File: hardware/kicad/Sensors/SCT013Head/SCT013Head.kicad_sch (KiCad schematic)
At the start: 7 parts, among them J1 Conn_01x05_Pin

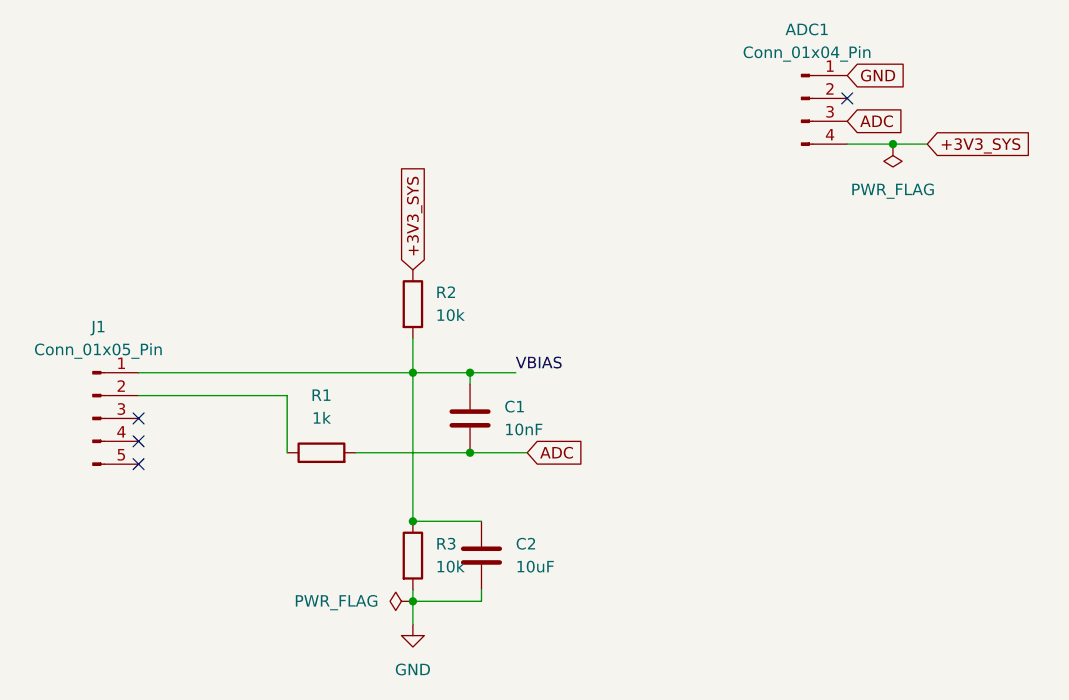
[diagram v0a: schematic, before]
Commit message: hardware(sct013): correct tip connection and label ADC port
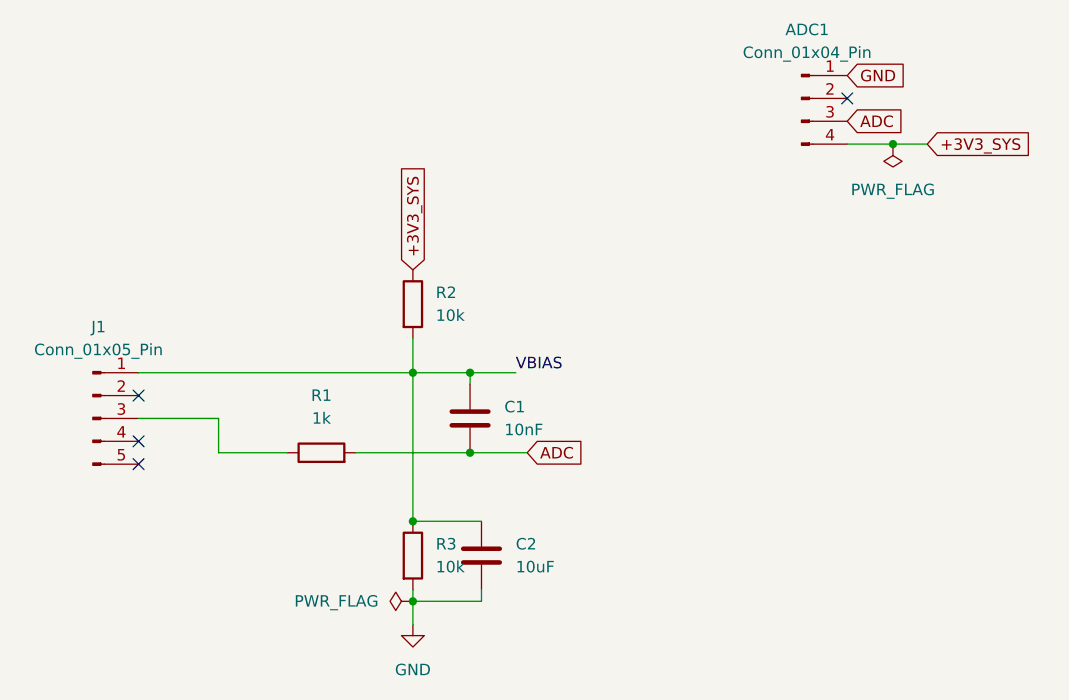
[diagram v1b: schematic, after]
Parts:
- ADC1: footprint Connector_Wire:SolderWire-0.25sqmm_1x04_P4.2mm_D0.65mm_OD1.7mm -> Connector_PinHeader_2.54mm:PinHeader_1x04_P2.54mm_Vertical
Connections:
- net at J1.2 (Pin_2): no longer R1.1
- net at J1.3 (Pin_3): now also R1.1
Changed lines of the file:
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@@
 	)
 	(no_connect
-		(at 68.58 96.52)
+		(at 68.58 93.98)
 	)
 	(no_connect
@@
 	(wire
 		(pts
-			(xy 85.09 93.98) (xy 85.09 100.33)
+			(xy 68.58 96.52) (xy 77.47 96.52)
 		)
 		(stroke
@@
 	(wire
 		(pts
+			(xy 77.47 96.52) (xy 77.47 100.33)
+		)
+		(stroke
+			(width 0)
+			(type default)
+		)
+	)
+	(wire
+		(pts
 			(xy 105.41 100.33) (xy 111.76 100.33)
 		)
@@
 	(wire
 		(pts
-			(xy 68.58 93.98) (xy 85.09 93.98)
+			(xy 77.47 100.33) (xy 85.09 100.33)
 		)
 		(stroke
@@
 			)
 		)
-		(property "Footprint" "Connector_Wire:SolderWire-0.25sqmm_1x04_P4.2mm_D0.65mm_OD1.7mm"
+		(property "Footprint" "Connector_PinHeader_2.54mm:PinHeader_1x04_P2.54mm_Vertical"
 			(at 142.24 60.96 0)
 			(hide yes)

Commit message: hardware(sct013): add input attenuator and update kit parts
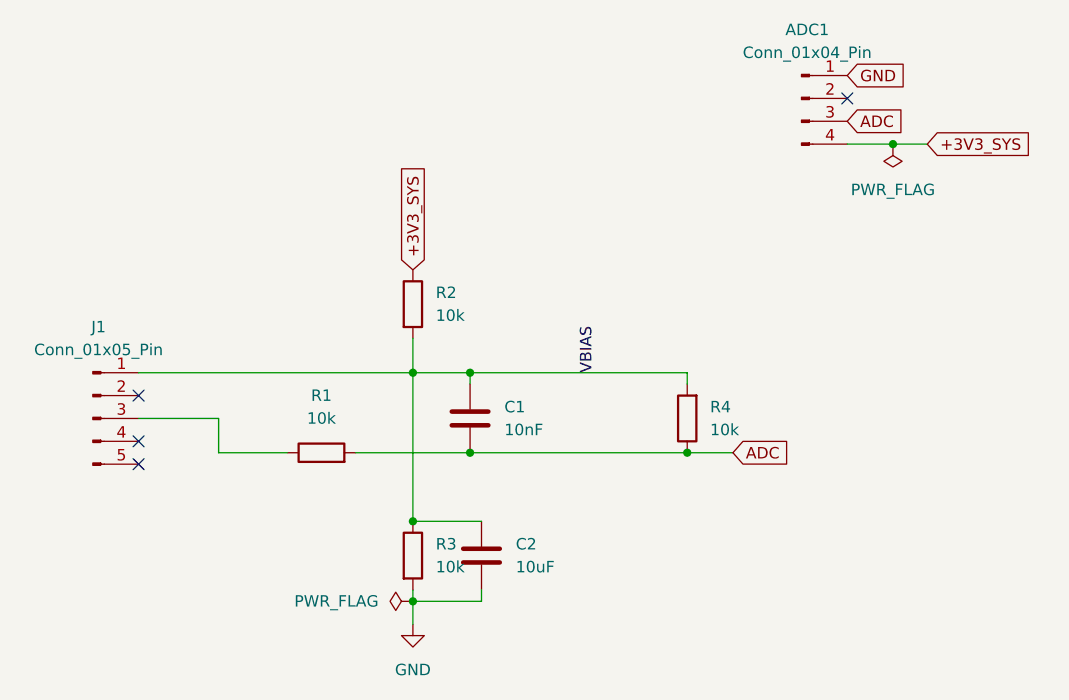
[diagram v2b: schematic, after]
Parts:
- added R4: 10k, Resistor_SMD:R_1206_3216Metric_Pad1.30x1.75mm_HandSolder, symbol Device:R
- R1: value 1k -> 10k
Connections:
- net ADC: now also R4.1
- net VBIAS: now also R4.2
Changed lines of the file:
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@@
+	)
+	(junction
+		(at 129.54 100.33)
+		(diameter 0)
+		(color 0 0 0 0)
 	)
 	(junction
@@
 	(wire
 		(pts
+			(xy 129.54 91.44) (xy 129.54 92.71)
+		)
+		(stroke
+			(width 0)
+			(type default)
+		)
+	)
+	(wire
+		(pts
+			(xy 129.54 100.33) (xy 134.62 100.33)
+		)
+		(stroke
+			(width 0)
+			(type default)
+		)
+	)
+	(wire
+		(pts
 			(xy 99.06 115.57) (xy 99.06 116.84)
 		)
@@
 	(wire
 		(pts
-			(xy 105.41 100.33) (xy 111.76 100.33)
+			(xy 105.41 100.33) (xy 129.54 100.33)
 		)
 		(stroke
@@
 	(wire
 		(pts
-			(xy 105.41 91.44) (xy 110.49 91.44)
+			(xy 105.41 91.44) (xy 129.54 91.44)
 		)
 		(stroke
@@
 	)
 	(label "VBIAS"
-		(at 110.49 91.44 0)
+		(at 119.38 91.44 90)
 		(effects
 			(font
@@
 	(global_label "ADC"
 		(shape input)
-		(at 111.76 100.33 0)
+		(at 134.62 100.33 0)
 		(fields_autoplaced yes)
 		(effects
@@
 		)
 		(property "Intersheetrefs" "${INTERSHEET_REFS}"
-			(at 118.3738 100.33 0)
+			(at 141.2338 100.33 0)
 			(hide yes)
 			(show_name no)
@@
 		(dnp no)
 		(fields_autoplaced yes)
-		(property "Reference" "#FLG01"
+		(property "Reference" "#FLG02"
 			(at 152.4 67.945 0)
 			(hide yes)
@@
 			(project "SCT013Head"
 				(path "/21b686d7-beef-4669-9055-5863613e214c"
-					(reference "#FLG01")
+					(reference "#FLG02")
 					(unit 1)
 				)
@@
 		(dnp no)
 		(fields_autoplaced yes)
-		(property "Reference" "#FLG02"
+		(property "Reference" "#FLG01"
 			(at 97.155 116.84 0)
 			(hide yes)
@@
 			(project "SCT013Head"
 				(path "/21b686d7-beef-4669-9055-5863613e214c"
-					(reference "#FLG02")
+					(reference "#FLG01")
 					(unit 1)
 				)
@@
 	(symbol
 		(lib_id "Device:R")
+		(at 129.54 96.52 180)
+		(unit 1)
+		(body_style 1)
+		(exclude_from_sim no)
+		(in_bom yes)
+		(on_board yes)
+		(in_pos_files yes)
+		(dnp no)
+		(fields_autoplaced yes)
+		(property "Reference" "R4"
+			(at 132.08 95.2499 0)
+			(show_name no)
+			(do_not_autoplace no)
+			(effects
+				(font
+					(size 1.27 1.27)
+				)
+				(justify right)
+			)
+		)
+		(property "Value" "10k"
+			(at 132.08 97.7899 0)
+			(show_name no)
+			(do_not_autoplace no)
+			(effects
+				(font
+					(size 1.27 1.27)
+				)
+				(justify right)
+			)
+		)
+		(property "Footprint" "Resistor_SMD:R_1206_3216Metric_Pad1.30x1.75mm_HandSolder"
+			(at 131.318 96.52 90)
+			(hide yes)
+			(show_name no)
+			(do_not_autoplace no)
+			(effects
+				(font
+					(size 1.27 1.27)
+				)
+			)
+		)
+		(property "Datasheet" ""
+			(at 129.54 96.52 0)
+			(hide yes)
+			(show_name no)
+			(do_not_autoplace no)
+			(effects
+				(font
+					(size 1.27 1.27)
+				)
+			)
+		)
+		(property "Description" "Resistor"
+			(at 129.54 96.52 0)
+			(hide yes)
+			(show_name no)
+			(do_not_autoplace no)
+			(effects
+				(font
+					(size 1.27 1.27)
+				)
+			)
+		)
+		(pin "1"
+		)
+		(pin "2"
+		)
+		(instances
+			(project "SCT013Head"
+				(path "/21b686d7-beef-4669-9055-5863613e214c"
+					(reference "R4")
+					(unit 1)
+				)
+			)
+		)
+	)
+	(symbol
+		(lib_id "Device:R")
 		(at 88.9 100.33 90)
 		(unit 1)
@@
 			)
 		)
-		(property "Value" "1k"
+		(property "Value" "10k"
 			(at 88.9 96.52 90)
 			(show_name no)
